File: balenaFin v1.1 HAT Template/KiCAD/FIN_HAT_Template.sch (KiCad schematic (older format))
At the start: 6 parts, among them J1 Raspberry_Pi_2_3, J2 POE_Header, J3 Co-Processor_Header, J4 USB_Header

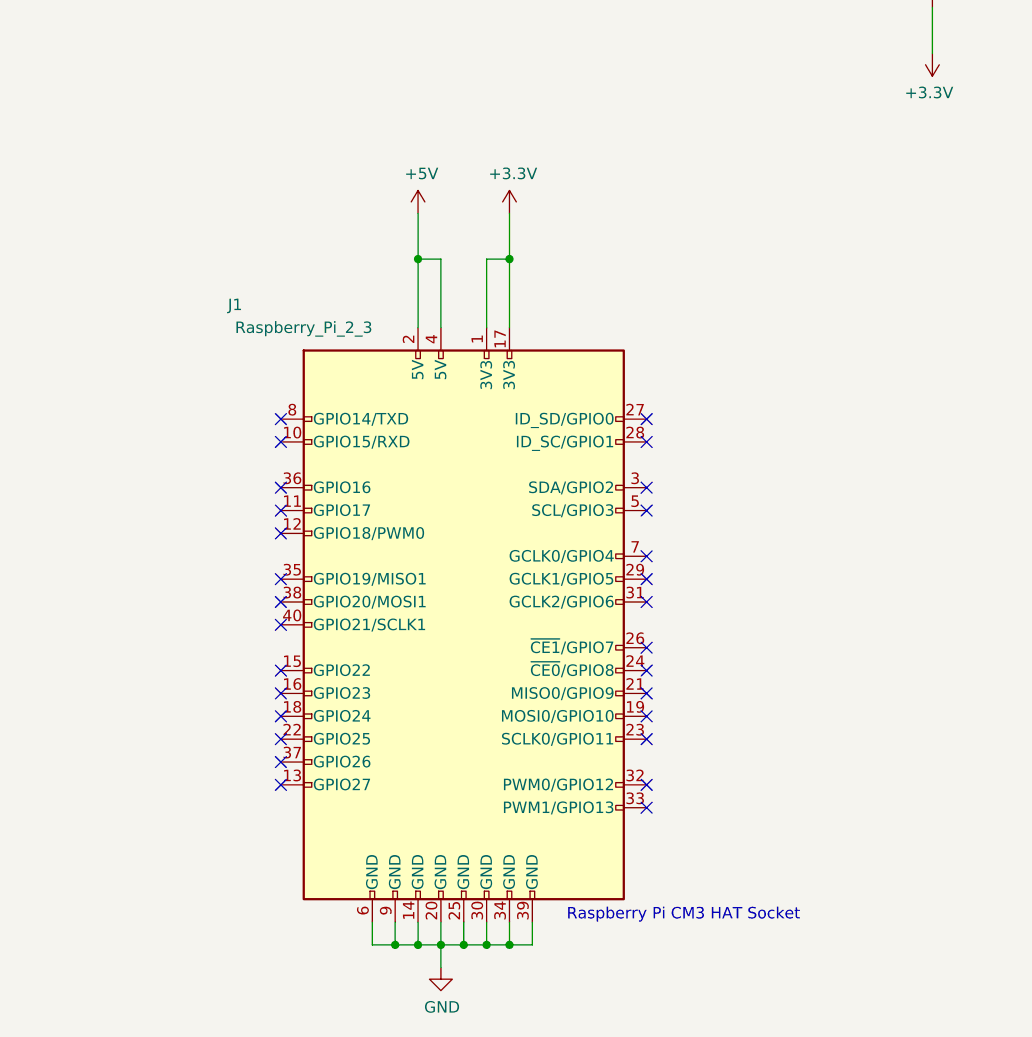
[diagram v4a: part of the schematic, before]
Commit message: Modified the RaspberryPi Header to match the physical header pinout
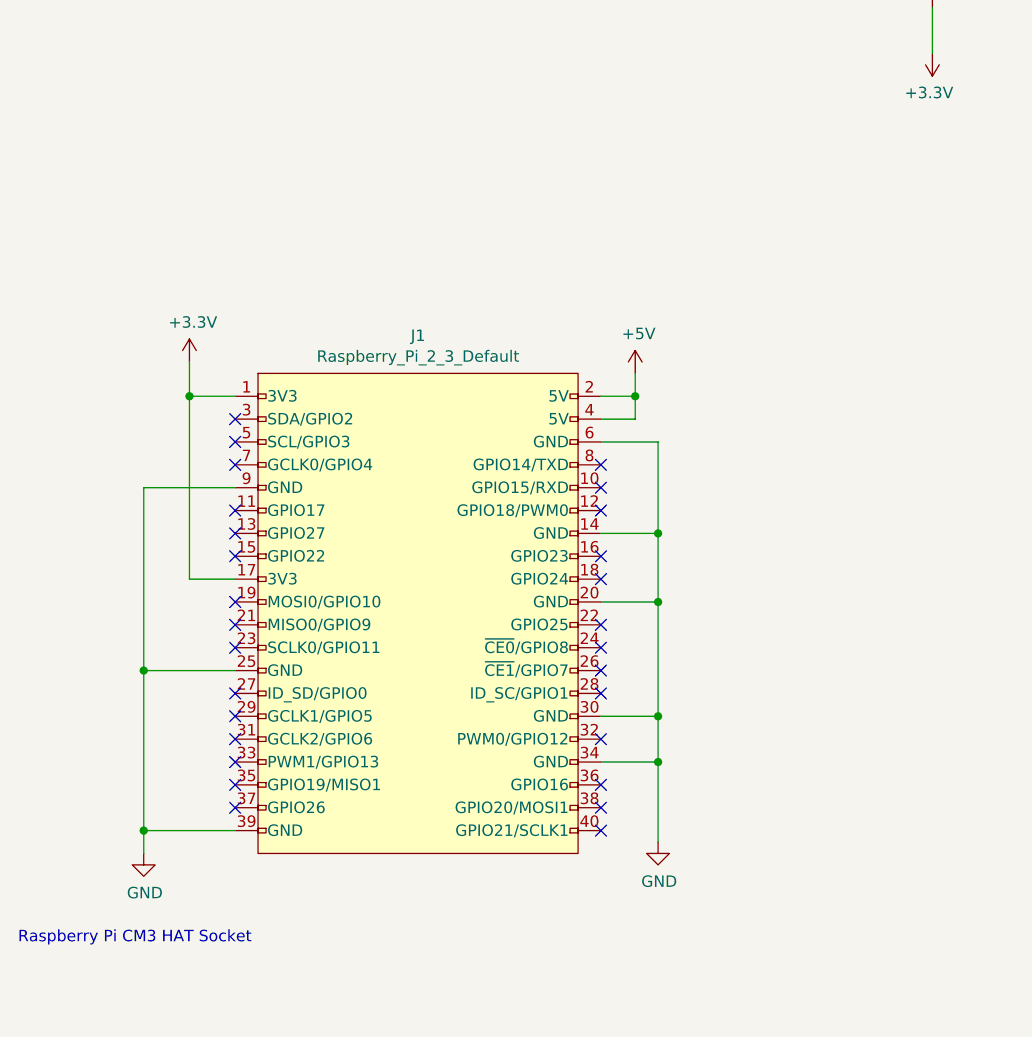
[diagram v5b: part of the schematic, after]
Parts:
- removed J1: Raspberry_Pi_2_3, FIN HAT Template:PinSocket_2x20_P2.54mm_Vertical, symbol FIN_HAT_TEMPLATE:Raspberry_Pi_2_3
- added J1: Raspberry_Pi_2_3_Default, FIN HAT Template:PinSocket_2x20_P2.54mm_Vertical, symbol FIN_HAT_TEMPLATE:Raspberry_Pi_2_3_Default
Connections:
- net +3V3: now also J1.1 (3V3), J1.17 (3V3)
- net +5V: now also J1.2 (5V), J1.4 (5V)
- net GND: now also J1.14 (GND), J1.20 (GND), J1.25 (GND), J1.30 (GND), J1.34 (GND), J1.39 (GND), J1.6 (GND), J1.9 (GND)
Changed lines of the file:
@@
-	1    0    0    -1
-$EndComp
-Text Notes 4000 5100 0    50   ~ 0
-Raspberry Pi CM3 HAT Socket
-$Comp
-L power:+3.3V #PWR03
-U 1 1 5F07F1C6
-P 3750 2000
-F 0 "#PWR03" H 3750 1850 50  0001 C CNN
-F 1 "+3.3V" H 3765 2173 50  0000 C CNN
-F 2 "" H 3750 2000 50  0001 C CNN
-F 3 "" H 3750 2000 50  0001 C CNN
-	1    3750 2000
-	1    0    0    -1
-$EndComp
-$Comp
-L power:+5V #PWR01
-U 1 1 5F07F8B1
-P 3350 2000
-F 0 "#PWR01" H 3350 1850 50  0001 C CNN
-F 1 "+5V" H 3365 2173 50  0000 C CNN
-F 2 "" H 3350 2000 50  0001 C CNN
-F 3 "" H 3350 2000 50  0001 C CNN
-	1    3350 2000
-	1    0    0    -1
-$EndComp
-$Comp
-L power:GND #PWR02
-U 1 1 5F07D099
-P 3450 5300
-F 0 "#PWR02" H 3450 5050 50  0001 C CNN
-F 1 "GND" H 3455 5127 50  0000 C CNN
-F 2 "" H 3450 5300 50  0001 C CNN
-F 3 "" H 3450 5300 50  0001 C CNN
-	1    3450 5300
-	1    0    0    -1
-$EndComp
-Wire Wire Line
-	3350 2000 3350 2200
-Wire Wire Line
-	3750 2000 3750 2200
-Wire Wire Line
-	3750 2200 3750 2500
-Connection ~ 3750 2200
-Wire Wire Line
-	3650 2200 3750 2200
-Wire Wire Line
-	3650 2500 3650 2200
-Wire Wire Line
-	3450 2200 3450 2500
-Wire Wire Line
-	3350 2200 3450 2200
-Connection ~ 3350 2200
-Wire Wire Line
-	3350 2500 3350 2200
-Wire Wire Line
-	3750 5200 3850 5200
-Connection ~ 3750 5200
-Wire Wire Line
-	3750 5100 3750 5200
-Wire Wire Line
-	3650 5200 3750 5200
-Connection ~ 3650 5200
-Wire Wire Line
-	3650 5100 3650 5200
-Wire Wire Line
-	3550 5200 3650 5200
-Connection ~ 3550 5200
-Wire Wire Line
-	3550 5100 3550 5200
-Wire Wire Line
-	3250 5100 3250 5200
-Wire Wire Line
-	3250 5200 3350 5200
-Connection ~ 3350 5200
-Wire Wire Line
-	3350 5100 3350 5200
-Wire Wire Line
-	3450 5300 3450 5200
-Wire Wire Line
-	3350 5200 3450 5200
-Wire Wire Line
-	3450 5200 3550 5200
-Connection ~ 3450 5200
-Wire Wire Line
-	3450 5100 3450 5200
-Wire Wire Line
-	3850 5200 3850 5100
-Connection ~ 3250 5200
-Wire Wire Line
-	3150 5200 3250 5200
-Wire Wire Line
-	3150 5100 3150 5200
-NoConn ~ 2750 4500
-NoConn ~ 2750 4400
-NoConn ~ 2750 4300
-NoConn ~ 2750 4200
-NoConn ~ 2750 4100
-NoConn ~ 2750 4000
-NoConn ~ 2750 3800
-NoConn ~ 2750 3700
-NoConn ~ 2750 3600
-NoConn ~ 2750 3400
-NoConn ~ 2750 3300
-NoConn ~ 2750 3200
-NoConn ~ 2750 3000
-NoConn ~ 2750 2900
-NoConn ~ 4350 4600
-NoConn ~ 4350 4500
-NoConn ~ 4350 4300
-NoConn ~ 4350 4200
-NoConn ~ 4350 4100
-NoConn ~ 4350 4000
-NoConn ~ 4350 3900
-NoConn ~ 4350 3700
-NoConn ~ 4350 3600
-NoConn ~ 4350 3500
-NoConn ~ 4350 3300
-NoConn ~ 4350 3200
-NoConn ~ 4350 3000
-NoConn ~ 4350 2900
-$Comp
-L FIN_HAT_TEMPLATE:Raspberry_Pi_2_3 J1
-U 1 1 5F15F5E4
-P 3550 3800
-F 0 "J1" H 2550 5200 50  0000 C CNN
-F 1 "Raspberry_Pi_2_3" H 2850 5100 50  0000 C CNN
-F 2 "FIN HAT Template:PinSocket_2x20_P2.54mm_Vertical" H 3550 3800 50  0001 C CNN
-F 3 "https://www.raspberrypi.org/documentation/hardware/raspberrypi/schematics/rpi_SCH_3bplus_1p0_reduced.pdf" H 3550 3800 50  0001 C CNN
-	1    3550 3800
 	1    0    0    -1
 $EndComp
@@
 	1    0    0    -1
 $EndComp
+$Comp
+L power:GND #PWR02
+U 1 1 5F07D099
+P 2150 4800
+F 0 "#PWR02" H 2150 4550 50  0001 C CNN
+F 1 "GND" H 2155 4627 50  0000 C CNN
+F 2 "" H 2150 4800 50  0001 C CNN
+F 3 "" H 2150 4800 50  0001 C CNN
+	1    2150 4800
+	1    0    0    -1
+$EndComp
+$Comp
+L power:+3.3V #PWR03
+U 1 1 5F07F1C6
+P 2350 2650
+F 0 "#PWR03" H 2350 2500 50  0001 C CNN
+F 1 "+3.3V" H 2365 2823 50  0000 C CNN
+F 2 "" H 2350 2650 50  0001 C CNN
+F 3 "" H 2350 2650 50  0001 C CNN
+	1    2350 2650
+	1    0    0    -1
+$EndComp
+$Comp
+L power:+5V #PWR01
+U 1 1 5F07F8B1
+P 4300 2700
+F 0 "#PWR01" H 4300 2550 50  0001 C CNN
+F 1 "+5V" H 4315 2873 50  0000 C CNN
+F 2 "" H 4300 2700 50  0001 C CNN
+F 3 "" H 4300 2700 50  0001 C CNN
+	1    4300 2700
+	1    0    0    -1
+$EndComp
+Text Notes 1600 5200 0    50   ~ 0
+Raspberry Pi CM3 HAT Socket
+NoConn ~ 4150 3100
+NoConn ~ 2550 2900
+NoConn ~ 2550 3100
+NoConn ~ 4150 3200
+NoConn ~ 2550 3400
+NoConn ~ 2550 3500
+NoConn ~ 2550 3000
+NoConn ~ 2550 3800
+NoConn ~ 2550 3900
+NoConn ~ 4150 3300
+NoConn ~ 2550 4100
+NoConn ~ 2550 4200
+NoConn ~ 2550 4400
+NoConn ~ 2550 3300
+NoConn ~ 2550 4300
+NoConn ~ 2550 4500
+NoConn ~ 4150 3500
+NoConn ~ 4150 3600
+NoConn ~ 4150 3800
+NoConn ~ 4150 4000
+NoConn ~ 4150 4100
+NoConn ~ 4150 4300
+NoConn ~ 4150 4500
+NoConn ~ 4150 4600
+NoConn ~ 4150 4700
+NoConn ~ 2550 4600
+NoConn ~ 2550 3700
+NoConn ~ 4150 3900
+Wire Wire Line
+	2550 3200 2150 3200
+Wire Wire Line
+	2150 3200 2150 4000
+Wire Wire Line
+	2550 4700 2150 4700
+Connection ~ 2150 4700
+Wire Wire Line
+	2150 4700 2150 4800
+Wire Wire Line
+	2550 4000 2150 4000
+Connection ~ 2150 4000
+Wire Wire Line
+	2150 4000 2150 4700
+Wire Wire Line
+	2550 3600 2350 3600
+Wire Wire Line
+	2350 3600 2350 2800
+Wire Wire Line
+	4150 2900 4300 2900
+Wire Wire Line
+	4300 2900 4300 2800
+Wire Wire Line
+	4300 2800 4150 2800
+Wire Wire Line
+	4300 2800 4300 2700
+Connection ~ 4300 2800
+$Comp
+L power:GND #PWR0101
+U 1 1 5F190035
+P 4400 4750
+F 0 "#PWR0101" H 4400 4500 50  0001 C CNN
+F 1 "GND" H 4405 4577 50  0000 C CNN
+F 2 "" H 4400 4750 50  0001 C CNN
+F 3 "" H 4400 4750 50  0001 C CNN
+	1    4400 4750
+	1    0    0    -1
+$EndComp
+Wire Wire Line
+	4400 4750 4400 4400
+Wire Wire Line
+	4400 4400 4150 4400
+Wire Wire Line
+	4150 4200 4400 4200
+Wire Wire Line
+	4400 4200 4400 4400
+Connection ~ 4400 4400
+Wire Wire Line
+	4150 3700 4400 3700
+Wire Wire Line
+	4400 3700 4400 4200
+Connection ~ 4400 4200
+Wire Wire Line
+	4150 3400 4400 3400
+Wire Wire Line
+	4400 3400 4400 3700
+Connection ~ 4400 3700
+Wire Wire Line
+	4150 3000 4400 3000
+Wire Wire Line
+	4400 3000 4400 3400
+Connection ~ 4400 3400
+Wire Wire Line
+	2350 2800 2550 2800
+Wire Wire Line
+	2350 2650 2350 2800
+Connection ~ 2350 2800
+$Comp
+L FIN_HAT_TEMPLATE:Raspberry_Pi_2_3_Default J1
+U 1 1 5F1866CE
+P 2650 2800
+F 0 "J1" H 3350 3065 50  0000 C CNN
+F 1 "Raspberry_Pi_2_3_Default" H 3350 2974 50  0000 C CNN
+F 2 "FIN HAT Template:PinSocket_2x20_P2.54mm_Vertical" H 2650 2800 50  0001 C CNN
+F 3 "https://www.raspberrypi.org/documentation/hardware/raspberrypi/schematics/rpi_SCH_3bplus_1p0_reduced.pdf" H 2650 2800 50  0001 C CNN
+	1    2650 2800
+	1    0    0    -1
+$EndComp
